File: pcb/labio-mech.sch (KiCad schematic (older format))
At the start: 6 parts

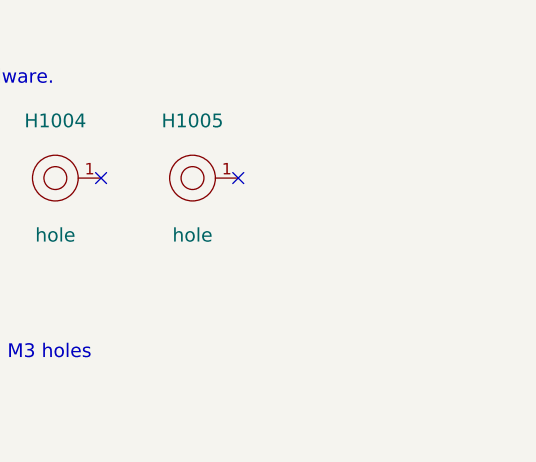
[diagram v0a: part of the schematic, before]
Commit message: expand outline to 175x85mm. move screen zif connector to top
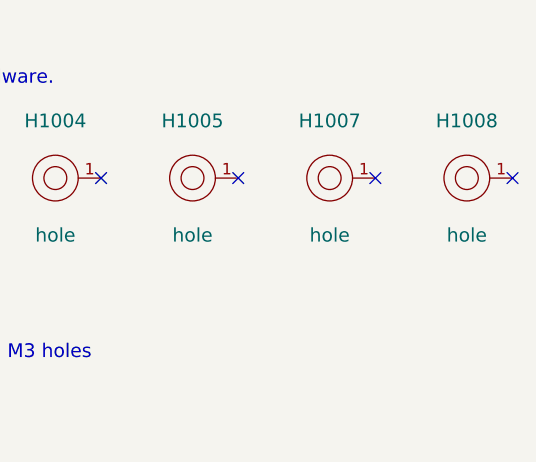
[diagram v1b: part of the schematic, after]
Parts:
- added H1007, H1008: hole, labio-special:hole-m3, symbol hole
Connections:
- no-connect marks 6 -> 8
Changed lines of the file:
@@
 NoConn ~ 2200 3100
 NoConn ~ 1600 3100
+$Comp
+L hole H1007
+U 1 1 578EDB90
+P 3800 1900
+F 0 "H1007" H 3800 2150 60  0000 C CNN
+F 1 "hole" H 3800 1650 60  0000 C CNN
+F 2 "labio-special:hole-m3" H 3800 1900 60  0001 C CNN
+F 3 "" H 3800 1900 60  0000 C CNN
+	1    3800 1900
+	1    0    0    -1
+$EndComp
+$Comp
+L hole H1008
+U 1 1 578EDB96
+P 4400 1900
+F 0 "H1008" H 4400 2150 60  0000 C CNN
+F 1 "hole" H 4400 1650 60  0000 C CNN
+F 2 "labio-special:hole-m3" H 4400 1900 60  0001 C CNN
+F 3 "" H 4400 1900 60  0000 C CNN
+	1    4400 1900
+	1    0    0    -1
+$EndComp
+NoConn ~ 4000 1900
+NoConn ~ 4600 1900
 $EndSCHEMATC

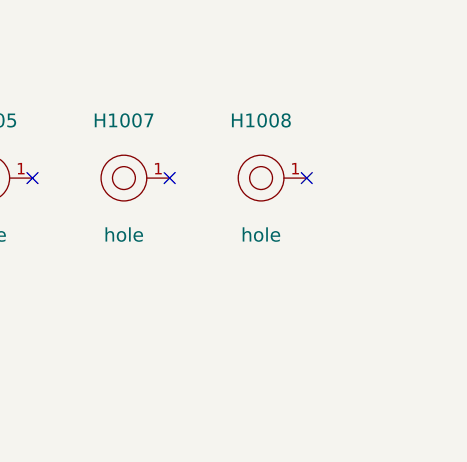
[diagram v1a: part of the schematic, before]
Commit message: shrink board to 85x150mm with tab board under rpi 0/debugger
* use space under rpi 0/debugger for imu since no visibility is needed
* rearrange dpad buttons and speaker to be more compact
* use 3V3_EXTRA for i2c pullups for consistency
* add bottom right hole to match future power module
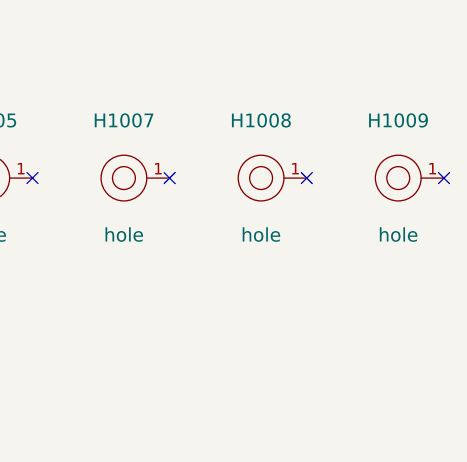
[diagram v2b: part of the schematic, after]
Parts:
- added H1009: hole, labio-special:hole-m3, symbol hole
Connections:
- no-connect marks 8 -> 9
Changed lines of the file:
@@
 NoConn ~ 4000 1900
 NoConn ~ 4600 1900
+$Comp
+L hole H1009
+U 1 1 579067D9
+P 5000 1900
+F 0 "H1009" H 5000 2150 60  0000 C CNN
+F 1 "hole" H 5000 1650 60  0000 C CNN
+F 2 "labio-special:hole-m3" H 5000 1900 60  0001 C CNN
+F 3 "" H 5000 1900 60  0000 C CNN
+	1    5000 1900
+	1    0    0    -1
+$EndComp
+NoConn ~ 5200 1900
 $EndSCHEMATC

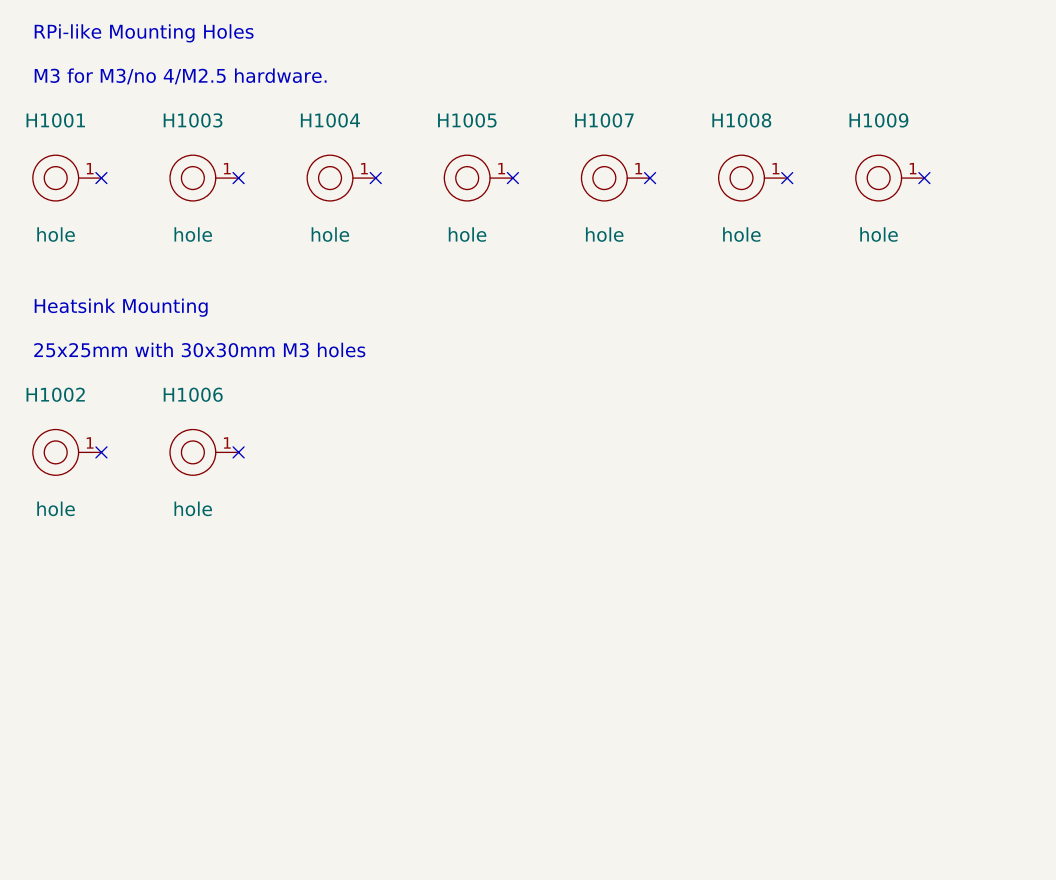
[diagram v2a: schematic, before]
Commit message: add cmu + wise logos, clean up silk, review for final errors
* move audio jack in so copper pads are inside board
* add logos/identifier text on silk and copper
* change rpi connector for no paste (to be left depopulated at fab)
* change soldermask expansion to 2 mils/3 mils minimum width
* add labels for motor, ADC, codec headers
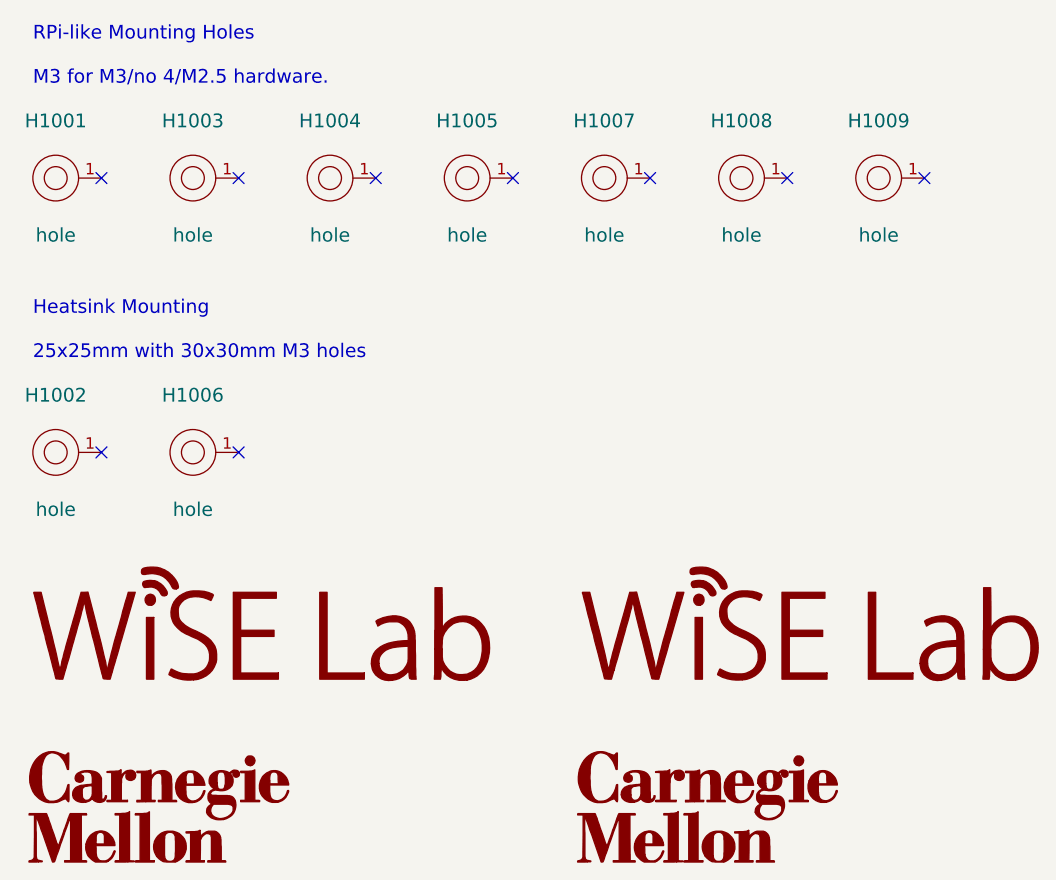
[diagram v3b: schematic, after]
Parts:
- added G1: CMU_LOGO, labio-special:cmu_logo_fsilk_3.7mm, symbol CMU_LOGO
- added G2: WISE_LOGO, labio-special:wise_logo_fsilk_2.5mm, symbol WISE_LOGO
- added G3: CMU_LOGO, labio-special:cmu_logo_fcu_3.7mm, symbol CMU_LOGO
- added G4: WISE_LOGO, labio-special:wise_logo_fcu_2.5mm, symbol WISE_LOGO
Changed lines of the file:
@@
 LIBS:valves
 LIBS:labio-special
+LIBS:wise_logo
+LIBS:cmu_logo
 LIBS:labio-cache
 EELAYER 25 0
@@
 $EndComp
 NoConn ~ 5200 1900
+$Comp
+L WISE_LOGO G2
+U 1 1 5795B82C
+P 2300 3850
+F 0 "G2" H 2300 3632 60  0001 C CNN
+F 1 "WISE_LOGO" H 2300 4068 60  0001 C CNN
+F 2 "labio-special:wise_logo_fsilk_2.5mm" H 2300 3850 60  0001 C CNN
+F 3 "" H 2300 3850 60  0000 C CNN
+	1    2300 3850
+	1    0    0    -1
+$EndComp
+$Comp
+L WISE_LOGO G4
+U 1 1 5795B859
+P 4700 3850
+F 0 "G4" H 4700 3632 60  0001 C CNN
+F 1 "WISE_LOGO" H 4700 4068 60  0001 C CNN
+F 2 "labio-special:wise_logo_fcu_2.5mm" H 4700 3850 60  0001 C CNN
+F 3 "" H 4700 3850 60  0000 C CNN
+	1    4700 3850
+	1    0    0    -1
+$EndComp
+$Comp
+L CMU_LOGO G1
+U 1 1 5795B878
+P 1850 4650
+F 0 "G1" H 1850 4439 60  0001 C CNN
+F 1 "CMU_LOGO" H 1850 4861 60  0001 C CNN
+F 2 "labio-special:cmu_logo_fsilk_3.7mm" H 1850 4650 60  0001 C CNN
+F 3 "" H 1850 4650 60  0000 C CNN
+	1    1850 4650
+	1    0    0    -1
+$EndComp
+$Comp
+L CMU_LOGO G3
+U 1 1 5795B8A5
+P 4250 4650
+F 0 "G3" H 4250 4439 60  0001 C CNN
+F 1 "CMU_LOGO" H 4250 4861 60  0001 C CNN
+F 2 "labio-special:cmu_logo_fcu_3.7mm" H 4250 4650 60  0001 C CNN
+F 3 "" H 4250 4650 60  0000 C CNN
+	1    4250 4650
+	1    0    0    -1
+$EndComp
 $EndSCHEMATC
